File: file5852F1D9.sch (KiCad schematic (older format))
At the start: 16 parts

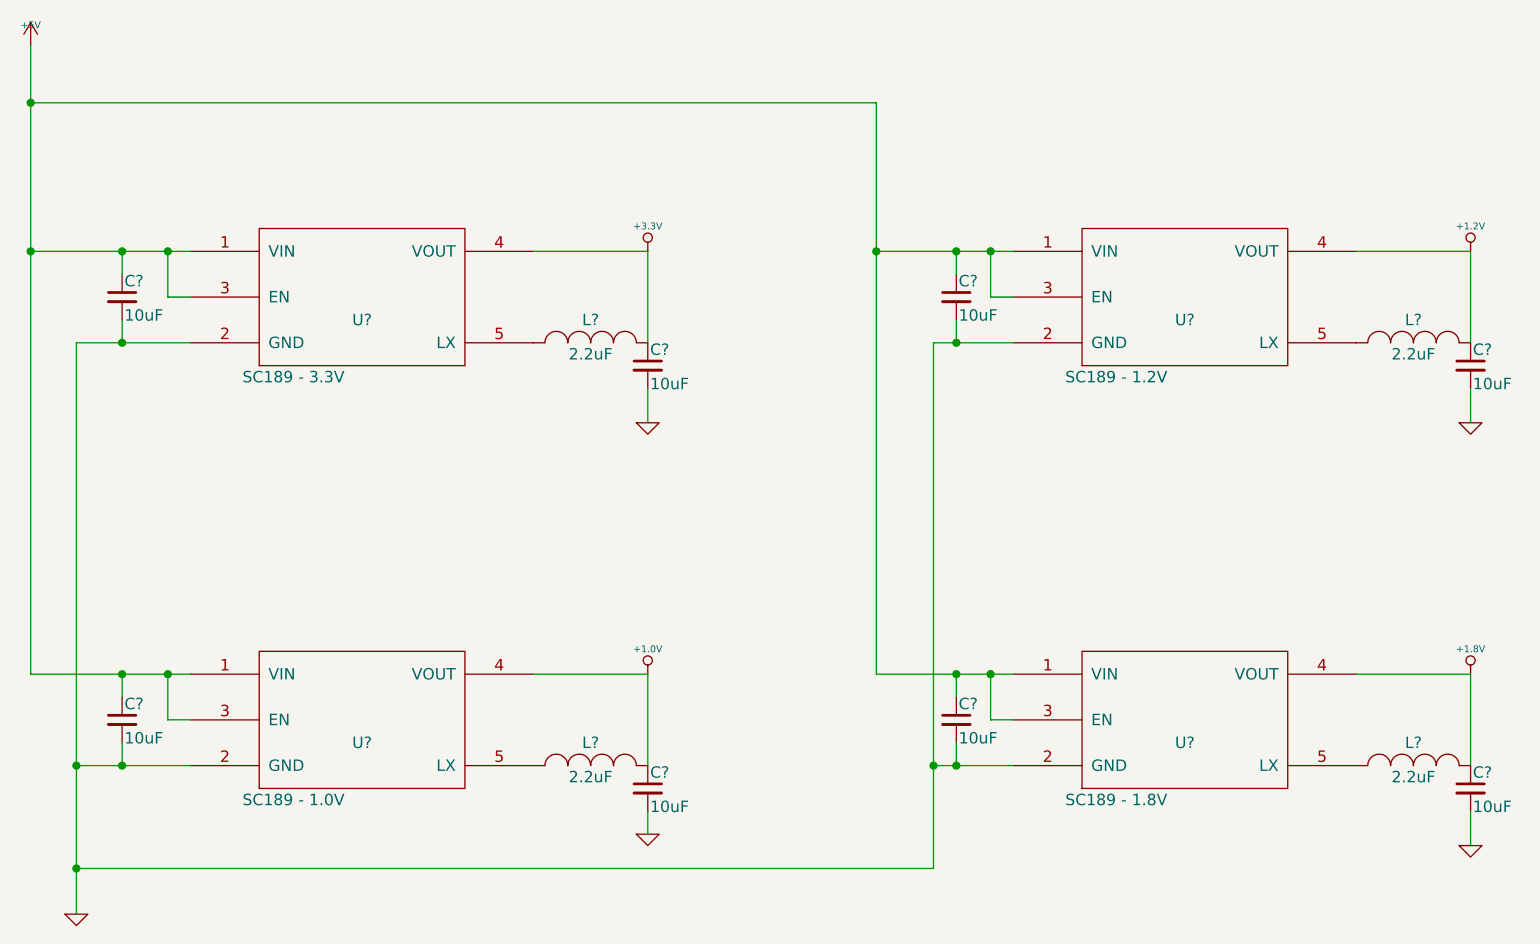
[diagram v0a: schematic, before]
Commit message: added HDMI, moved rotary encoders to USBSPI gpio
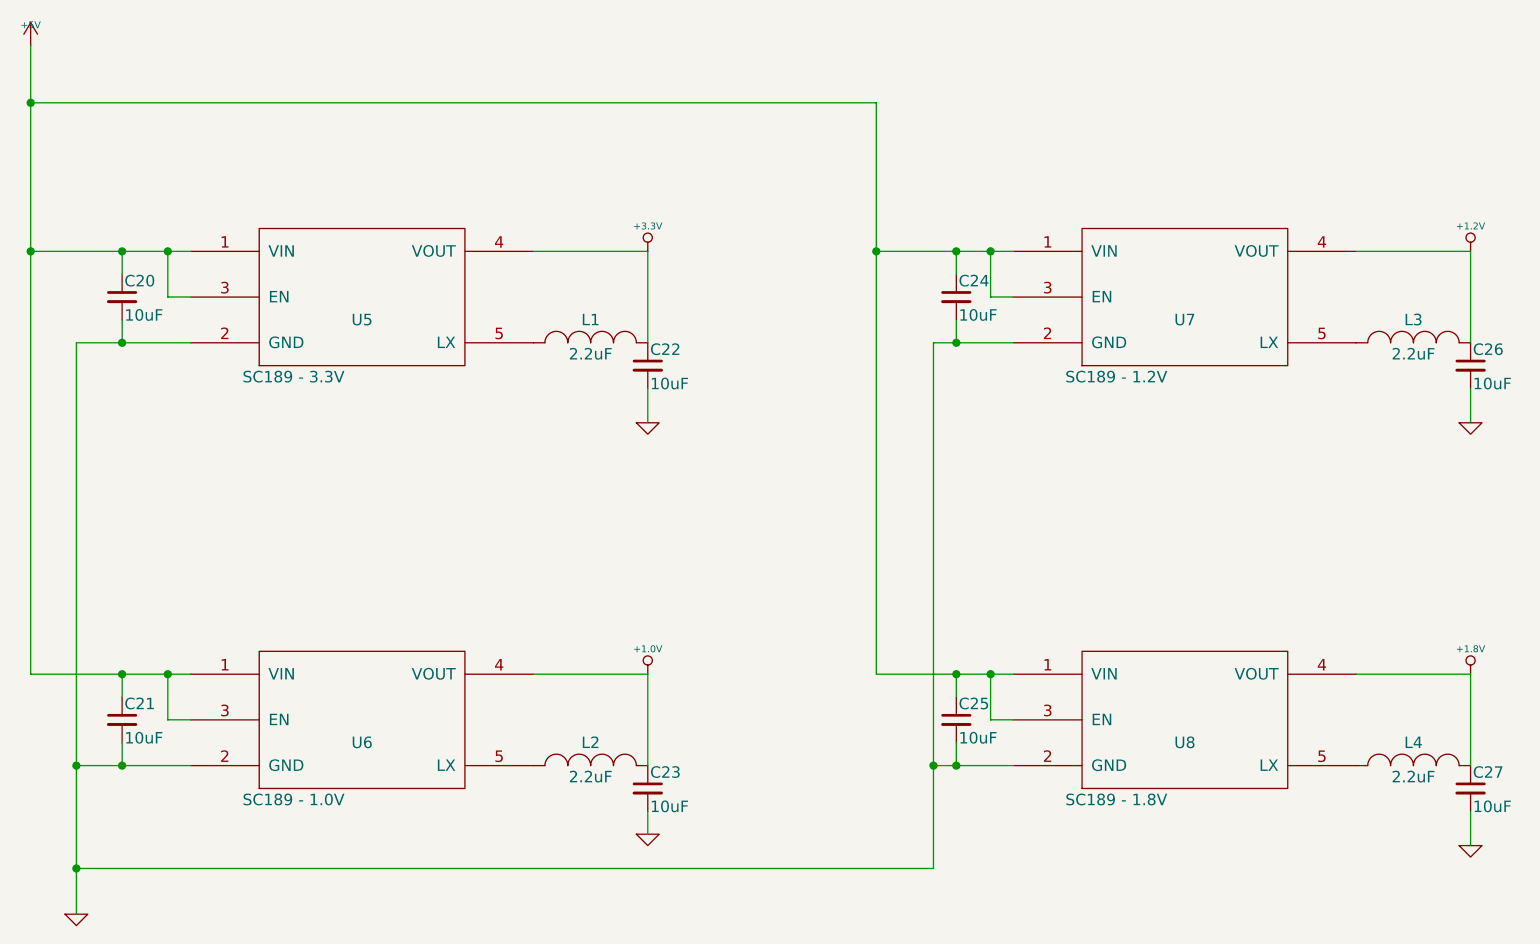
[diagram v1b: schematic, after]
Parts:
- gave numbers to parts that had none: 16
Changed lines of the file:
@@
 LIBS:usb_condom_extended_v1-cache
 LIBS:tinkerforge
+LIBS:si570
+LIBS:hdmi_BiDir_n
 EELAYER 25 0
 EELAYER END
 $Descr A4 11693 8268
 encoding utf-8
-Sheet 9 13
+Sheet 11 14
 Title ""
 Date ""
@@
 $EndDescr
 $Comp
-L SC189 U?
+L SC189 U7
 U 1 1 5852F1EA
 P 8250 2950
-F 0 "U?" H 8250 2850 50  0000 C CNN
+F 0 "U7" H 8250 2850 50  0000 C CNN
 F 1 "SC189 - 1.2V" H 7950 2600 50  0000 C CNN
 F 2 "MODULE" H 7950 3300 50  0001 C CNN
@@
 $EndComp
 $Comp
-L SC189 U?
+L SC189 U8
 U 1 1 5852F28D
 P 8250 4800
-F 0 "U?" H 8250 4700 50  0000 C CNN
+F 0 "U8" H 8250 4700 50  0000 C CNN
 F 1 "SC189 - 1.8V" H 7950 4450 50  0000 C CNN
 F 2 "MODULE" H 7950 5150 50  0001 C CNN
@@
 $EndComp
 $Comp
-L SC189 U?
+L SC189 U5
 U 1 1 5852F314
 P 4650 2950
-F 0 "U?" H 4650 2850 50  0000 C CNN
+F 0 "U5" H 4650 2850 50  0000 C CNN
 F 1 "SC189 - 3.3V" H 4350 2600 50  0000 C CNN
 F 2 "MODULE" H 4350 3300 50  0001 C CNN
@@
 $EndComp
 $Comp
-L SC189 U?
+L SC189 U6
 U 1 1 5852F383
 P 4650 4800
-F 0 "U?" H 4650 4700 50  0000 C CNN
+F 0 "U6" H 4650 4700 50  0000 C CNN
 F 1 "SC189 - 1.0V" H 4350 4450 50  0000 C CNN
 F 2 "MODULE" H 4350 5150 50  0001 C CNN
@@
 $EndComp
 $Comp
-L +5V #PWR?
+L +5V #PWR054
 U 1 1 58592D53
 P 3200 1850
-F 0 "#PWR?" H 3200 1940 20  0001 C CNN
+F 0 "#PWR054" H 3200 1940 20  0001 C CNN
 F 1 "+5V" H 3200 1940 30  0000 C CNN
 F 2 "" H 3200 1850 60  0001 C CNN
@@
 Connection ~ 6900 2750
 $Comp
-L GND-RESCUE-DFTBoard #PWR?
+L GND-RESCUE-DFTBoard #PWR055
 U 1 1 58592DBB
 P 3400 5650
-F 0 "#PWR?" H 3400 5650 30  0001 C CNN
+F 0 "#PWR055" H 3400 5650 30  0001 C CNN
 F 1 "GND" H 3400 5580 30  0001 C CNN
 F 2 "" H 3400 5650 60  0001 C CNN
@@
 Connection ~ 7400 4600
 $Comp
-L C_Small C?
+L C_Small C20
 U 1 1 58592EB2
 P 3600 2950
-F 0 "C?" H 3610 3020 50  0000 L CNN
+F 0 "C20" H 3610 3020 50  0000 L CNN
 F 1 "10uF" H 3610 2870 50  0000 L CNN
 F 2 "" H 3600 2950 50  0000 C CNN
@@
 $EndComp
 $Comp
-L C_Small C?
+L C_Small C24
 U 1 1 58592F69
 P 7250 2950
-F 0 "C?" H 7260 3020 50  0000 L CNN
+F 0 "C24" H 7260 3020 50  0000 L CNN
 F 1 "10uF" H 7260 2870 50  0000 L CNN
 F 2 "" H 7250 2950 50  0000 C CNN
@@
 $EndComp
 $Comp
-L C_Small C?
+L C_Small C25
 U 1 1 58592F8A
 P 7250 4800
-F 0 "C?" H 7260 4870 50  0000 L CNN
+F 0 "C25" H 7260 4870 50  0000 L CNN
 F 1 "10uF" H 7260 4720 50  0000 L CNN
 F 2 "" H 7250 4800 50  0000 C CNN
@@
 $EndComp
 $Comp
-L C_Small C?
+L C_Small C21
 U 1 1 58592FAD
 P 3600 4800
-F 0 "C?" H 3610 4870 50  0000 L CNN
+F 0 "C21" H 3610 4870 50  0000 L CNN
 F 1 "10uF" H 3610 4720 50  0000 L CNN
 F 2 "" H 3600 4800 50  0000 C CNN
@@
 Connection ~ 7250 5000
 $Comp
-L C_Small C?
+L C_Small C22
 U 1 1 5859393B
 P 5900 3250
-F 0 "C?" H 5910 3320 50  0000 L CNN
+F 0 "C22" H 5910 3320 50  0000 L CNN
 F 1 "10uF" H 5910 3170 50  0000 L CNN
 F 2 "" H 5900 3250 50  0000 C CNN
@@
 $EndComp
 $Comp
-L C_Small C?
+L C_Small C23
 U 1 1 58593A1D
 P 5900 5100
-F 0 "C?" H 5910 5170 50  0000 L CNN
+F 0 "C23" H 5910 5170 50  0000 L CNN
 F 1 "10uF" H 5910 5020 50  0000 L CNN
 F 2 "" H 5900 5100 50  0000 C CNN
@@
 $EndComp
 $Comp
-L C_Small C?
+L C_Small C26
 U 1 1 58593B07
 P 9500 3250
-F 0 "C?" H 9510 3320 50  0000 L CNN
+F 0 "C26" H 9510 3320 50  0000 L CNN
 F 1 "10uF" H 9510 3170 50  0000 L CNN
 F 2 "" H 9500 3250 50  0000 C CNN
@@
 $EndComp
 $Comp
-L C_Small C?
+L C_Small C27
 U 1 1 58593BBA
 P 9500 5100
-F 0 "C?" H 9510 5170 50  0000 L CNN
+F 0 "C27" H 9510 5170 50  0000 L CNN
 F 1 "10uF" H 9510 5020 50  0000 L CNN
 F 2 "" H 9500 5100 50  0000 C CNN
@@
 $EndComp
 $Comp
-L INDUCTOR_SMALL L?
+L INDUCTOR_SMALL L2
 U 1 1 58593D26
 P 5650 5000
-F 0 "L?" H 5650 5100 50  0000 C CNN
+F 0 "L2" H 5650 5100 50  0000 C CNN
 F 1 "2.2uF" H 5650 4950 50  0000 C CNN
 F 2 "" H 5650 5000 50  0000 C CNN
@@
 $EndComp
 $Comp
-L INDUCTOR_SMALL L?
+L INDUCTOR_SMALL L1
 U 1 1 58593E06
 P 5650 3150
-F 0 "L?" H 5650 3250 50  0000 C CNN
+F 0 "L1" H 5650 3250 50  0000 C CNN
 F 1 "2.2uF" H 5650 3100 50  0000 C CNN
 F 2 "" H 5650 3150 50  0000 C CNN
@@
 $EndComp
 $Comp
-L INDUCTOR_SMALL L?
+L INDUCTOR_SMALL L3
 U 1 1 58593E9A
 P 9250 3150
-F 0 "L?" H 9250 3250 50  0000 C CNN
+F 0 "L3" H 9250 3250 50  0000 C CNN
 F 1 "2.2uF" H 9250 3100 50  0000 C CNN
 F 2 "" H 9250 3150 50  0000 C CNN
@@
 $EndComp
 $Comp
-L INDUCTOR_SMALL L?
+L INDUCTOR_SMALL L4
 U 1 1 58593F31
 P 9250 5000
-F 0 "L?" H 9250 5100 50  0000 C CNN
+F 0 "L4" H 9250 5100 50  0000 C CNN
 F 1 "2.2uF" H 9250 4950 50  0000 C CNN
 F 2 "" H 9250 5000 50  0000 C CNN
@@
 	9500 4600 9500 5000
 $Comp
-L GND-RESCUE-DFTBoard #PWR?
+L GND-RESCUE-DFTBoard #PWR056
 U 1 1 58594786
 P 5900 3500
-F 0 "#PWR?" H 5900 3500 30  0001 C CNN
+F 0 "#PWR056" H 5900 3500 30  0001 C CNN
 F 1 "GND" H 5900 3430 30  0001 C CNN
 F 2 "" H 5900 3500 60  0001 C CNN
@@
 $EndComp
 $Comp
-L GND-RESCUE-DFTBoard #PWR?
+L GND-RESCUE-DFTBoard #PWR057
 U 1 1 58594848
 P 5900 5300
-F 0 "#PWR?" H 5900 5300 30  0001 C CNN
+F 0 "#PWR057" H 5900 5300 30  0001 C CNN
 F 1 "GND" H 5900 5230 30  0001 C CNN
 F 2 "" H 5900 5300 60  0001 C CNN
@@
 	5900 5200 5900 5300
 $Comp
-L GND-RESCUE-DFTBoard #PWR?
+L GND-RESCUE-DFTBoard #PWR058
 U 1 1 58594C14
 P 9500 5350
-F 0 "#PWR?" H 9500 5350 30  0001 C CNN
+F 0 "#PWR058" H 9500 5350 30  0001 C CNN
 F 1 "GND" H 9500 5280 30  0001 C CNN
 F 2 "" H 9500 5350 60  0001 C CNN
@@
 $EndComp
 $Comp
-L GND-RESCUE-DFTBoard #PWR?
+L GND-RESCUE-DFTBoard #PWR059
 U 1 1 58594C4F
 P 9500 3500
-F 0 "#PWR?" H 9500 3500 30  0001 C CNN
+F 0 "#PWR059" H 9500 3500 30  0001 C CNN
 F 1 "GND" H 9500 3430 30  0001 C CNN
 F 2 "" H 9500 3500 60  0001 C CNN
@@
 	9500 5200 9500 5350
 $Comp
-L +3.3V-RESCUE-DFTBoard #PWR?
+L +3.3V-RESCUE-DFTBoard #PWR060
 U 1 1 585961A7
 P 5900 2750
-F 0 "#PWR?" H 5900 2710 30  0001 C CNN
+F 0 "#PWR060" H 5900 2710 30  0001 C CNN
 F 1 "+3.3V" H 5900 2860 30  0000 C CNN
 F 2 "" H 5900 2750 60  0001 C CNN
@@
 $EndComp
 $Comp
-L +1.2V #PWR?
+L +1.2V #PWR061
 U 1 1 585961DB
 P 9500 2750
-F 0 "#PWR?" H 9500 2890 20  0001 C CNN
+F 0 "#PWR061" H 9500 2890 20  0001 C CNN
 F 1 "+1.2V" H 9500 2860 30  0000 C CNN
 F 2 "" H 9500 2750 60  0001 C CNN
@@
 $EndComp
 $Comp
-L +1.0V #PWR?
+L +1.0V #PWR062
 U 1 1 5859729A
 P 5900 4600
-F 0 "#PWR?" H 5900 4560 30  0001 C CNN
+F 0 "#PWR062" H 5900 4560 30  0001 C CNN
 F 1 "+1.0V" H 5900 4710 30  0000 C CNN
 F 2 "" H 5900 4600 60  0001 C CNN
@@
 $EndComp
 $Comp
-L +1.8V #PWR?
+L +1.8V #PWR063
 U 1 1 5859769E
 P 9500 4600
-F 0 "#PWR?" H 9500 4740 20  0001 C CNN
+F 0 "#PWR063" H 9500 4740 20  0001 C CNN
 F 1 "+1.8V" H 9500 4710 30  0000 C CNN
 F 2 "" H 9500 4600 60  0001 C CNN
